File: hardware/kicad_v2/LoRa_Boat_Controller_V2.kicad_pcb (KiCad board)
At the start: 2 copper layers, 80 x 46 mm, 118 parts, among them J1 BATTERY XT30, J2 ESC, J3 SERVO, J4 LoRa RYLR998, J5 GNSS, J6 USB-C, J7 SWD, Q1 AO3401A, SW1 RESET, U1 STM32F446RET6, U2 R1240N001B-TR-FE, U3 TPS54202, U4 74AHCT1G125, U5 74AHCT1G125, U6 ICM-20948, U7 USBLC6-2SC6, U8 INA180A1, Y1 8MHz, Y2 32.768kHz

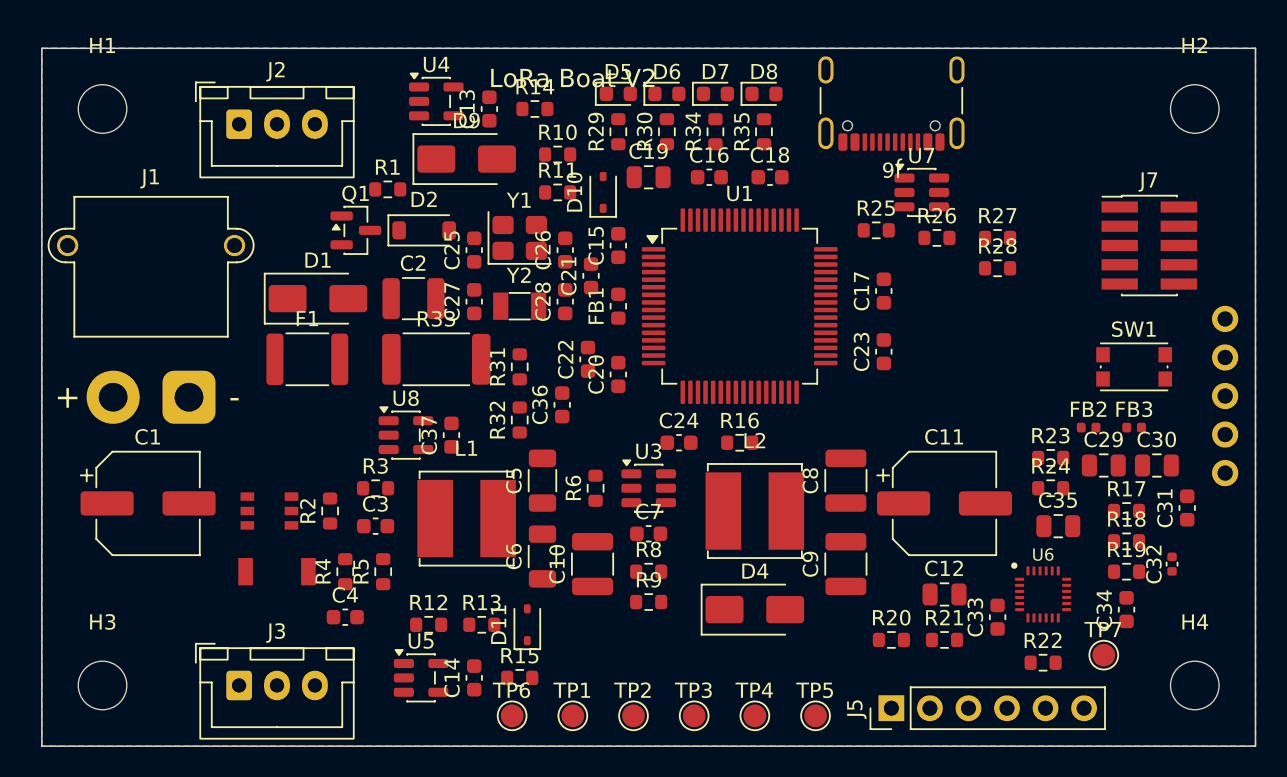
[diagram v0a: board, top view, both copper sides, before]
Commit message: Phase C: V2 board autorouted (freerouting 2.1.0, B.Cu GND plane), DRC 0 violations, priced BOM_V2, REPORT.md, V2 docs
- route_v2.py: DSN export with --gnd-plane bcu (freerouting drops a via next to every top-side GND pad), SES import, pour fill,
  GND stitch pass for pads the pours cannot reach (3 remain: J3-3, J5-2, J6 S1 - see HANDOFF pause note)
- netclasses retuned for the autorouter: Default 0.25 mm / 0.15 mm, Power 0.6 mm / 0.2 mm limited to coarse-pad nets;
  board rules 0.127 mm min; GND pours with solid pad connections (thermal 0.25/0.3 for the rest)
- board: 1074 track segments, 164 vias, 3 unconnected GND pins, 0 DRC violations; silkscreen title moved off the LEDs
- docs: docs/BOM_V2.csv (68 lines, $53.80 qty-1), REPORT.md (root), hardware/kicad_v2/README.md, README V2 section,
  V2_REQUIREMENTS REQ-MECH-01 / REQ-RF-05 / decision 7 for the 80 x 46 mm board, BLOCKERS decision-7 note,
  CONVERSION_LOG Phase C entry, docs index generator knows the V2 documents/images, V2 schematic SVGs + PDF
- PROMPT_FOR_CODEX.md rewritten for the v2-design branch (V2 viewer/atlas/review packets)

Co-Authored-By: Claude Fable 5.1 <noreply@anthropic.com>
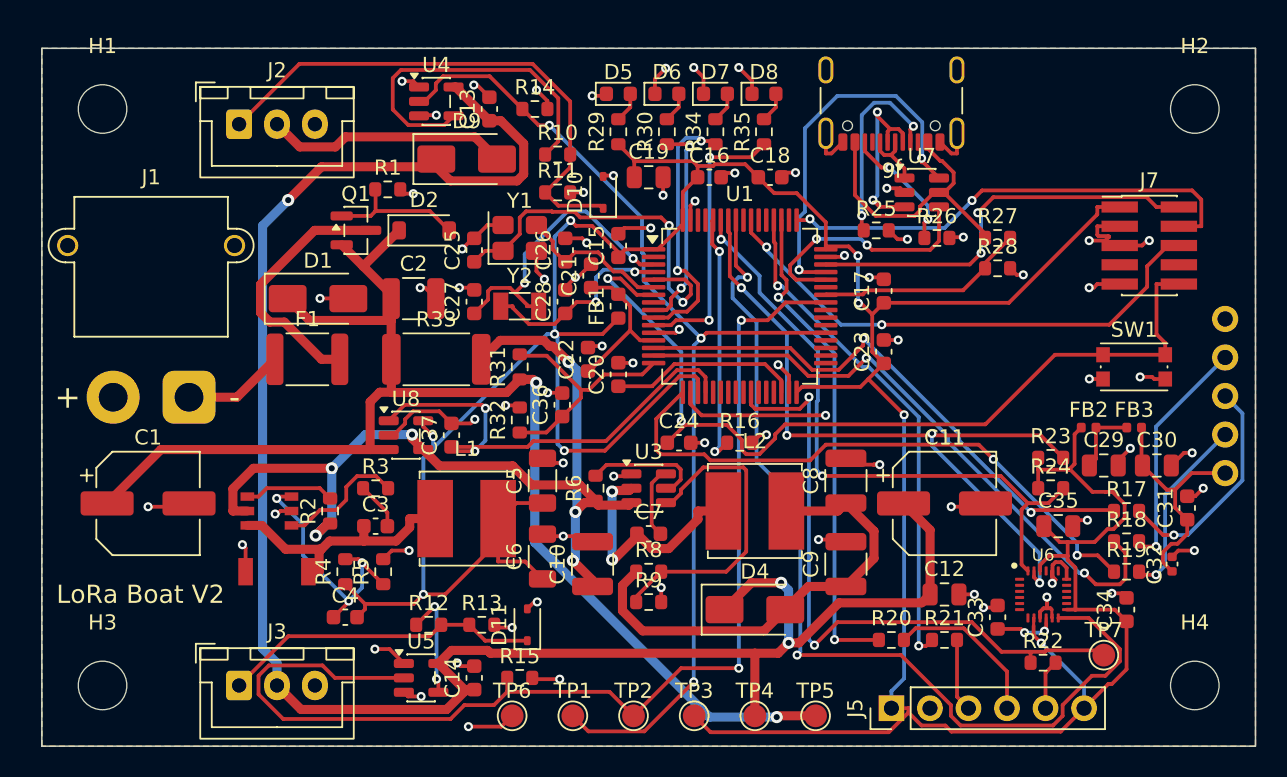
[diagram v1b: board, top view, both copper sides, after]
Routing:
- net +3V3: track 0.00 -> 244.3 mm, vias 0 -> 9
- net GND: track 0.00 -> 141.1 mm, vias 0 -> 73
- net VSERVO: track 0.00 -> 129.4 mm, vias 0 -> 3
- net VIN_RAW: track 0.00 -> 90.6 mm, vias 0 -> 2
- net PWM_SERVO_PA8: track 0.00 -> 76.4 mm, vias 0 -> 2
- net PWM_ESC_PC6: track 0.00 -> 70.0 mm, vias 0 -> 3
- net IMU_INT: track 0.00 -> 63.2 mm, vias 0 -> 2
- net VIN_BUCK: track 0.00 -> 62.7 mm, vias 0 -> 6
- net NRST: track 0.00 -> 59.0 mm, vias 0 -> 2
- net I2C1_SCL: track 0.00 -> 48.5 mm, vias 0 -> 4
- net PPS_PB0: track 0.00 -> 43.1 mm, vias 0 -> 2
- net I2C1_SDA: track 0.00 -> 41.6 mm, vias 0 -> 2
- net LORA_RX_PA1: track 0.00 -> 41.5 mm, vias 0 -> 2
- net LORA_NRST_PA3: track 0.00 -> 39.4 mm, vias 0 -> 2
- net LORA_TX_PA0: track 0.00 -> 37.2 mm, vias 0 -> 2
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
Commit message: Phase C draft closed: GND stitch pass, review fixes (U3 no-connect, D2 10 V, VBUS divider), renders, docs index, release notes
- route_v2.py: isolated GND clusters found by union-find over the filled pour outlines (joined through vias and THT pads),
  stitched with straight or L-shaped 0.25 mm tracks to the connected pour, accepted only when the unconnected count drops;
  1 of 3 islands stitched on this layout, 2 remain for hand-finish (documented in hardware/kicad_v2/README.md and REPORT.md)
- gen_v2.py: V2 no longer inherits the V1 FORCE_NC (TPS54202 pin 1 had a no-connect flag in the schematic); GND pours solid-connected
- v2_design.py: D2 BZT52C10 (10 V clamp, AO3401A Vgs max 12 V), R28 47k (PA9 sees 2.5 V), BOM 67 lines $53.80
- board: 1075 segments, 165 vias, DRC 0 violations, 2 unconnected; renders docs/img/v2_pcb_top/bottom.png, copper SVGs
- REPORT.md numbers filled in (35 V1 findings, routing stats); BLOCKERS decision-7 row updated; docs/INDEX.md regenerated with V2 entries;
  HANDOFF/AGENT_STATUS release note; CONVERSION_LOG entry

Co-Authored-By: Claude Fable 5.1 <noreply@anthropic.com>
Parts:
- D2: value 12V -> 10V
- R28: value 22k -> 47k
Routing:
- net GND: track 141.1 -> 142.5 mm, vias 73 -> 74
